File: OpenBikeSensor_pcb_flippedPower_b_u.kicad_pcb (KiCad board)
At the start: 2 copper layers, 58.2 x 62.2 mm, 34 parts, among them J1 Conn_01x02_Male, J10 Conn_02x03_Odd_Even, J11 Conn_01x02_Male, J2 Conn_01x04_Female, J3 Conn_01x04_Male, J4 Conn_01x04_Male, J5 Conn_01x05_Male, J6 Conn_01x02_Male, J7 Conn_01x06_Male, J8 Conn_01x06_Male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

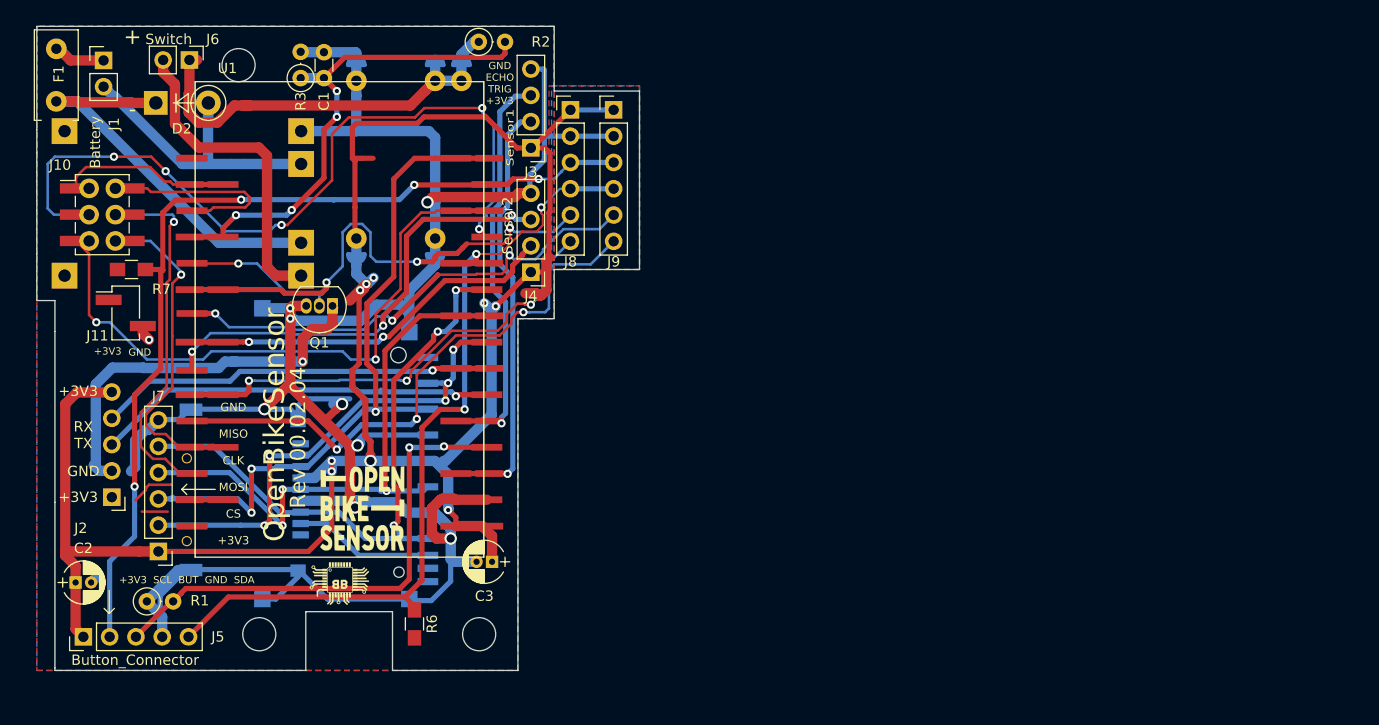
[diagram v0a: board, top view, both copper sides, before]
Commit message: add new US sensor boards to the PCB
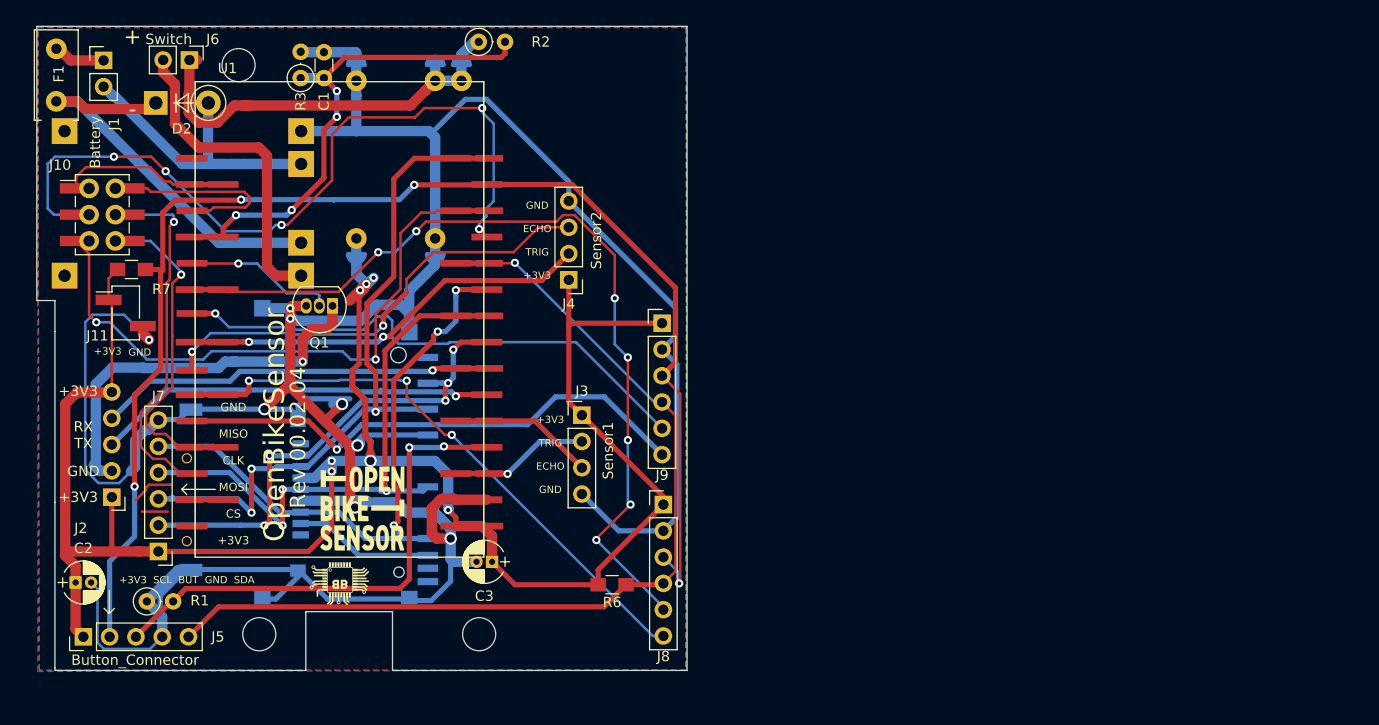
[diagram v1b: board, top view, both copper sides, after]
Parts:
- moved J8 39.2 mm to (82.8, 93.2)
- moved J3 26.3 mm to (74.9, 84.6), turned to 0 degrees
- moved J9 21.1 mm to (82.7, 75.7)
- moved R6 19.5 mm to (77.9, 101.0), turned to 180 degrees
- moved J4 3.74 mm to (73.7, 71.5)
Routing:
- net GND: track 263.4 -> 337.7 mm, vias 9 -> 8
- net SCL: track 90.5 -> 134.8 mm
- net GPIO_INT_1: track 48.5 -> 84.8 mm, vias 3 -> 7
- net TRIG1: track 41.6 -> 13.5 mm
- net ECHO1: track 39.0 -> 15.0 mm, vias 1 -> 0
- net +3V3: track 236.2 -> 223.8 mm, vias 9 -> 7
- net XSHUT_1: track 45.7 -> 58.1 mm
- net SDA: track 84.9 -> 93.7 mm, vias 3 -> 1
- net GPIO_INT_2: track 47.7 -> 52.2 mm, vias 3 -> 1
- net XSHUT_2: track 55.3 -> 51.4 mm, vias 3 -> 1
- net TRIG2: track 37.3 -> 40.2 mm
- net ECHO2: track 46.3 -> 44.6 mm, vias 3 -> 2
- net +BATT: track 38.2 -> 39.3 mm
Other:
- board size 58.2 x 62.2 mm -> 62.8 x 62.2 mm
- board text added: "+3V3 TRIG ECHO GND"

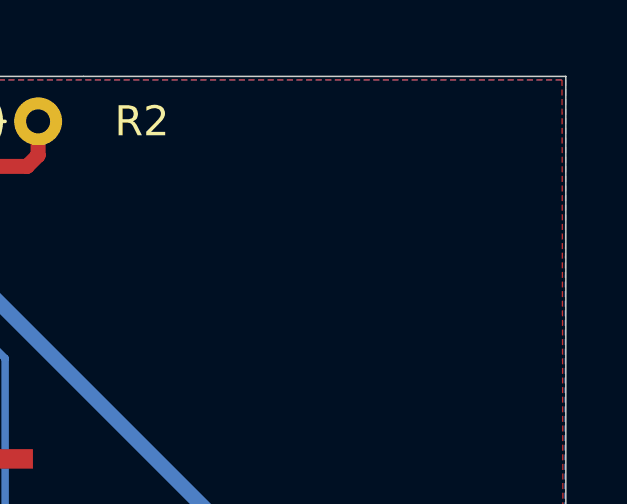
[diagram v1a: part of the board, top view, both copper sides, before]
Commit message: deleted 2 orphan traces
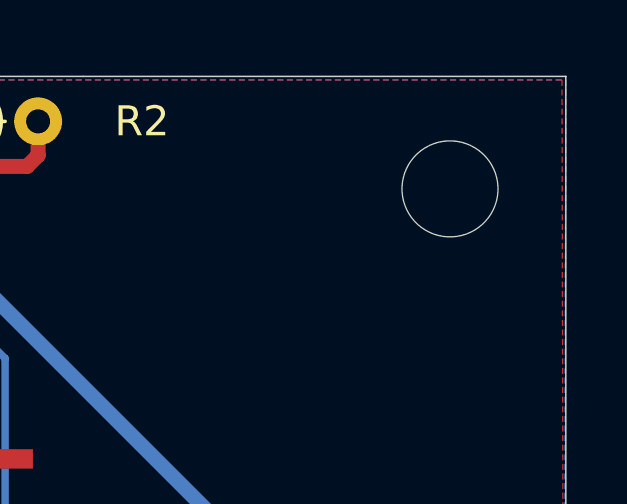
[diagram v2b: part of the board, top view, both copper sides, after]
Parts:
- added REF**: MountingHole_3.2mm_M3_DIN965, Mounting_Holes:MountingHole_3.2mm_M3_DIN965, F.Cu at (81.2, 50.7)
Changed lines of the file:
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@@
-(kicad_pcb (version 20171130) (host pcbnew "(5.1.6)-1")
+(kicad_pcb (version 20171130) (host pcbnew "(5.1.4)-1")
   (general
     (thickness 1.6)
@@
     (tracks 749)
     (zones 0)
-    (modules 34)
+    (modules 35)
     (nets 45)
   )
@@
   )
   (setup
-    (last_trace_width 1)
+    (last_trace_width 0.25)
     (user_trace_width 0.2)
     (user_trace_width 0.5)
@@
     (add_net XSHUT_1)
     (add_net XSHUT_2)
+  )
+  (module Mounting_Holes:MountingHole_3.2mm_M3_DIN965 locked (layer F.Cu)
+    (at 81.2292 50.7492)
+    (descr "Mounting Hole 3.2mm, no annular, M3, DIN965")
+    (tags "mounting hole 3.2mm no annular m3 din965")
+    (attr virtual)
+    (fp_text reference REF** (at 0 -3.8) (layer F.SilkS) hide
+      (effects (font (size 1 1) (thickness 0.15)))
+    )
+    (fp_text value MountingHole_3.2mm_M3_DIN965 (at 0 3.8) (layer F.Fab)
+      (effects (font (size 1 1) (thickness 0.15)))
+    )
+    (fp_text user %R (at 0.3 0) (layer F.Fab)
+      (effects (font (size 1 1) (thickness 0.15)))
+    )
+    (fp_circle (center 0 0) (end 3.05 0) (layer F.CrtYd) (width 0.05))
+    (fp_circle (center 0 0) (end 2.8 0) (layer Cmts.User) (width 0.15))
+    (pad 1 np_thru_hole circle (at 0 0) (size 3.2 3.2) (drill 3.2) (layers *.Cu *.Mask))
+    (model "${OPENBIKE}/hex_socket_button_head_M3x05 (1).step"
+      (at (xyz 0 0 0))
+      (scale (xyz 1 1 1))
+      (rotate (xyz 0 0 0))
+    )
   )
   (module Diodes_THT:D_DO-41_SOD81_P5.08mm_Vertical_KathodeUp (layer F.Cu)
@@
     )
     (pad 1 np_thru_hole circle (at 0 0) (size 3.2 3.2) (drill 3.2) (layers *.Cu *.Mask))
+    (model "${OPENBIKE}/hex_socket_button_head_M3x05 (1).step"
+      (at (xyz 0 0 0))
+      (scale (xyz 1 1 1))
+      (rotate (xyz 0 0 0))
+    )
   )
   (module Mounting_Holes:MountingHole_3.2mm_M3_DIN965 locked (layer F.Cu)
@@
     )
     (pad 1 np_thru_hole circle (at 0 0) (size 3.2 3.2) (drill 3.2) (layers *.Cu *.Mask))
+    (model "${OPENBIKE}/hex_socket_button_head_M3x05 (1).step"
+      (at (xyz 0 0 0))
+      (scale (xyz 1 1 1))
+      (rotate (xyz 0 0 0))
+    )
   )
   (module Mounting_Holes:MountingHole_3.2mm_M3_DIN965 locked (layer F.Cu)
@@
     )
     (pad 1 np_thru_hole circle (at 0 0) (size 3.2 3.2) (drill 3.2) (layers *.Cu *.Mask))
+    (model "${OPENBIKE}/hex_socket_button_head_M3x05 (1).step"
+      (at (xyz 0 0 0))
+      (scale (xyz 1 1 1))
+      (rotate (xyz 0 0 0))
+    )
   )
   (module SD_CARD:SD_CARD-XUNPU-SD-101_C266601 locked (layer B.Cu)

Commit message: new _u version
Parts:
- removed the REF** at (81.2, 50.7)
- removed the REF** at (41.8, 50.8)
- removed the REF** at (43.8, 105.8)
- added G***: LOGO, HLRS_LogoBack:HLRS_LogoBack, F.Cu at (80.3, 64.1)
- added G***: LOGO, HLRS_Logo:HLRS_Logo, F.Cu at (49.3, 109.1)
- D2: footprint Diodes_THT:D_DO-41_SOD81_P5.08mm_Vertical_KathodeUp -> Diode_THT:D_DO-41_SOD81_P10.16mm_Horizontal
- J5: footprint Pin_Headers:Pin_Header_Straight_1x05_Pitch2.54mm -> Connector_JST:JST_XH_B5B-XH-AM_1x05_P2.50mm_Vertical
- R1, R3: footprint Resistors_THT:R_Axial_DIN0207_L6.3mm_D2.5mm_P2.54mm_Vertical -> Resistor_THT:R_Axial_DIN0207_L6.3mm_D2.5mm_P10.16mm_Horizontal
- R2: footprint Resistors_THT:R_Axial_DIN0207_L6.3mm_D2.5mm_P2.54mm_Vertical -> Resistor_THT:R_Axial_DIN0207_L6.3mm_D2.5mm_P15.24mm_Horizontal
- moved REF** 55.4 mm to (82.9, 53.3)
- moved G*** 46.1 mm to (71.6, 55.4), turned to 270 degrees
- moved G*** 22.9 mm to (73.8, 95.9)
- moved G*** 20.7 mm to (72.0, 102.4), turned to 90 degrees
- moved R1 20.2 mm to (52.8, 105.7), turned to 180 degrees
- moved G*** 16.3 mm to (62.9, 107.1)
- moved C1 8.03 mm to (42.5, 49.0), turned to 180 degrees
- moved R6 3.94 mm to (77.9, 104.9)
- moved M1 1.82 mm to (35.2, 64.1)
- moved R3 1.71 mm to (49.4, 51.6), turned to 270 degrees
- moved J5 1.44 mm to (27.6, 107.2), turned to 0 degrees
- moved D2 1.25 mm to (32.5, 54.2)
- moved R2 0.87 mm to (65.8, 48.8), turned to 180 degrees
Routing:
- net TX: track 75.3 -> 52.2 mm, vias 5 -> 2
- net BUTTON: track 49.0 -> 61.5 mm
- net Net-(C1-Pad1): track 48.4 -> 39.2 mm, vias 4 -> 3
- net +3V3: track 223.8 -> 229.9 mm
- net SDA: track 93.7 -> 99.3 mm
- net Net-(J6-Pad2): track 31.2 -> 26.0 mm
- net +BATT: track 39.3 -> 35.8 mm
- net SCL: track 134.8 -> 131.5 mm
- net XSHUT_1: track 58.1 -> 60.0 mm
- net GND: track 337.7 -> 335.9 mm, vias 8 -> 10
- net -BATT: track 28.5 -> 27.4 mm
- net +VDC: track 41.2 -> 40.2 mm
- net GPIO_INT_2: track 52.2 -> 52.7 mm
- net GPS_GND_CONT: track 14.6 -> 14.2 mm, vias 1 -> 0
- net GPIO_INT_1: track 84.8 -> 85.1 mm, vias 7 -> 3
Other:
- board size 62.8 x 62.2 mm -> 65.7 x 64.6 mm
- board text added: "12"
- board text added: "13"
- board text added: "RX"
- board text added: "Rev 00.03.08"
- board text added: "TX"
- board text added: "VN"
- board text added: "VP"
- board text removed: "Rev 00.02.04"

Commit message: fixed boundary
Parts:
- removed the G*** at (80.3, 64.1)
- added G***: LOGO, HLRS_Logo:HLRS_LogoBack, F.Cu at (79.4, 63.9)

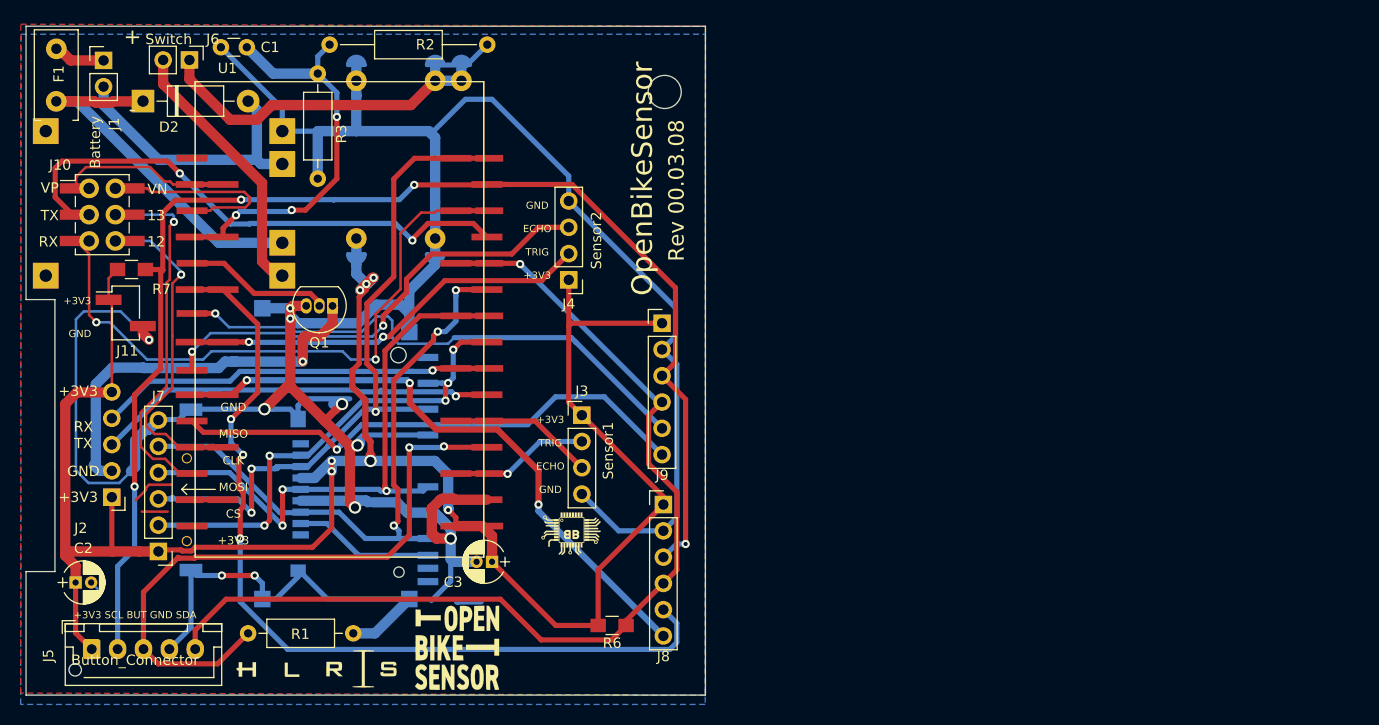
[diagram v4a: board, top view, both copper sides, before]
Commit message: added more srew holes improved ground/vcc planes updated 3D Models
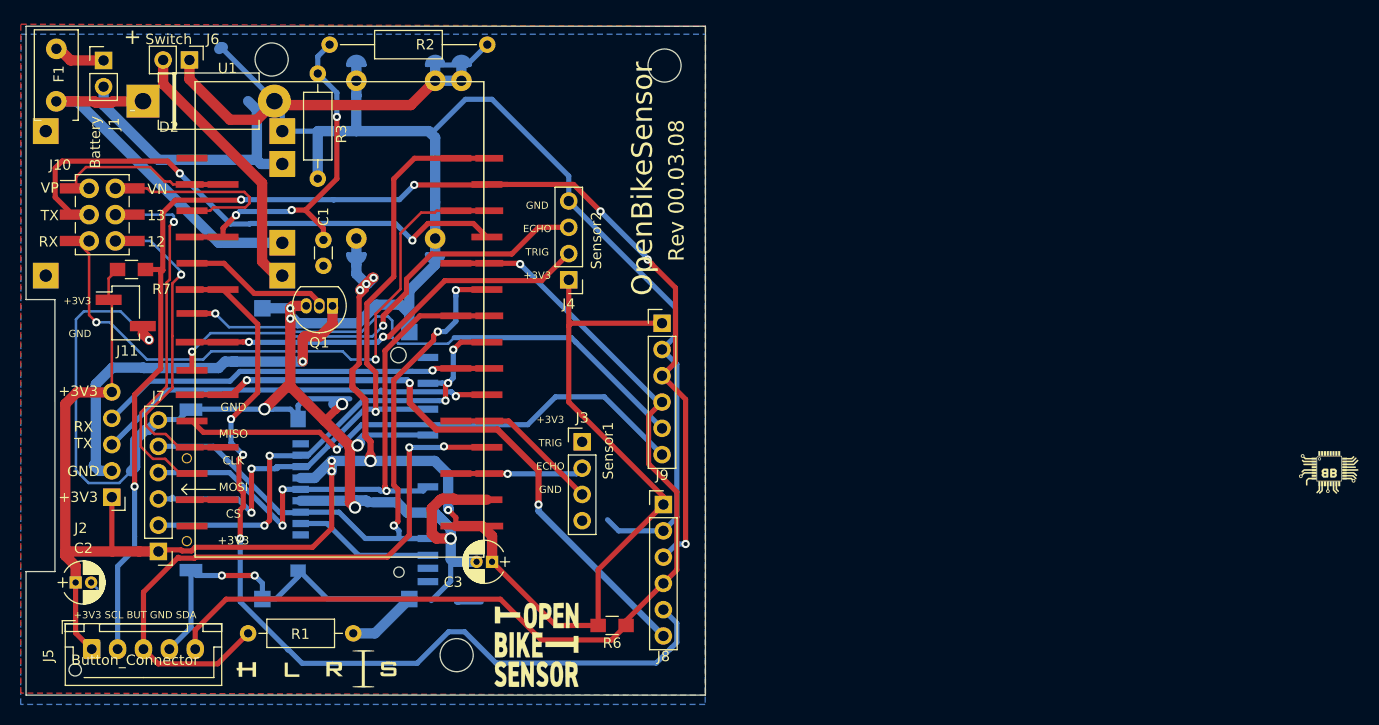
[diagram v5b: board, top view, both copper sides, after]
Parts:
- added REF**: MountingHole_3.2mm_M3_DIN965, Mounting_Holes:MountingHole_3.2mm_M3_DIN965, F.Cu at (44.9, 50.2)
- added REF**: MountingHole_3.2mm_M3_DIN965, Mounting_Holes:MountingHole_3.2mm_M3_DIN965, F.Cu at (62.8, 107.8)
- D2: footprint Diode_THT:D_DO-41_SOD81_P10.16mm_Horizontal -> Diode_THT:D_DO-201AD_P12.70mm_Horizontal
- moved G*** 73.5 mm to (147.0, 90.0)
- moved C1 20.0 mm to (49.9, 67.6), turned to 270 degrees
- moved G*** 7.68 mm to (70.5, 106.8)
- moved J3 2.58 mm to (75.0, 87.2)
- moved REF** 2.55 mm to (82.9, 50.8)
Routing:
- net (no net): track 6.64 -> 0.00 mm
- net Net-(C1-Pad1): track 39.2 -> 34.9 mm
- net GPIO_INT_1: track 85.1 -> 89.0 mm
- net GND: track 335.9 -> 332.4 mm
- net ECHO1: track 15.0 -> 16.1 mm
- net TRIG1: track 13.5 -> 12.4 mm
- net SCL: track 131.5 -> 131.6 mm, vias 4 -> 6

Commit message: fixed mistake in esp footprint fixed problem with diode
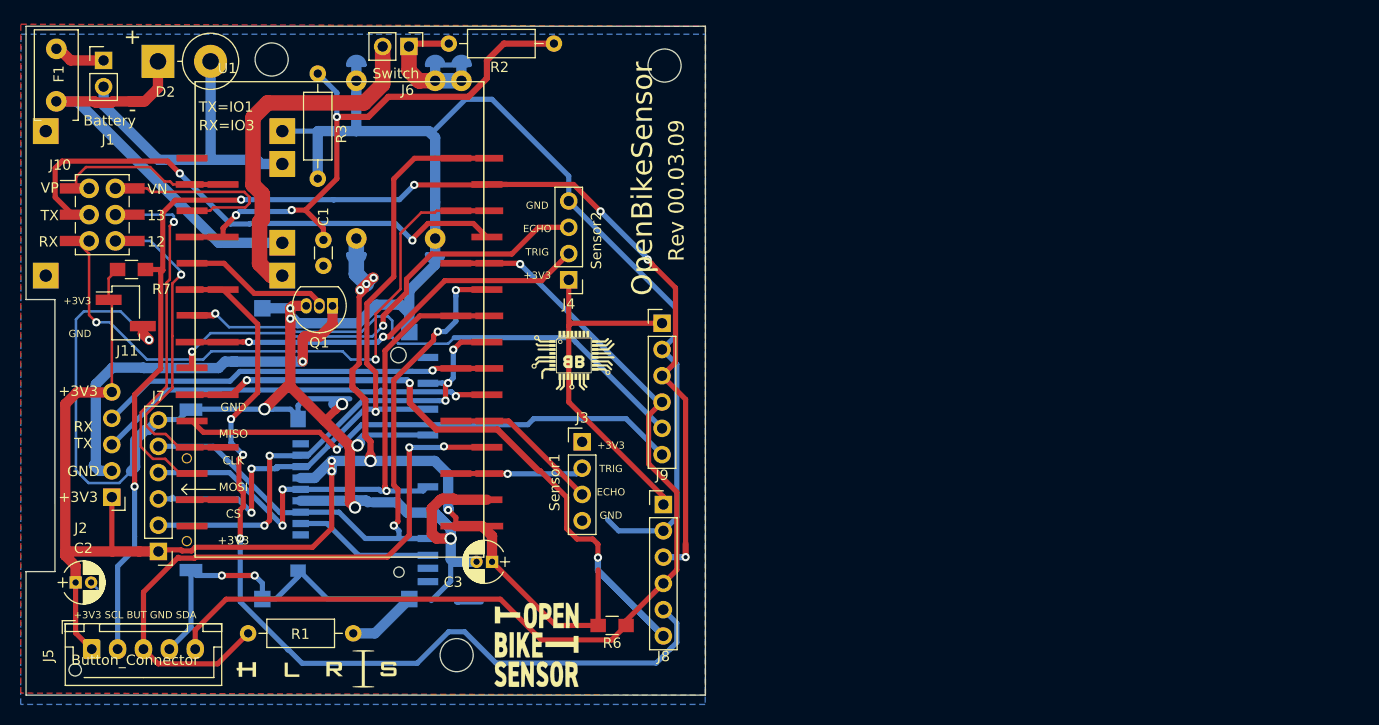
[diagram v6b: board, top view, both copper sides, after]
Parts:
- D2: footprint Diode_THT:D_DO-201AD_P12.70mm_Horizontal -> Diode_THT:D_DO-201AD_P5.08mm_Vertical_KathodeUp
- G***: footprint Custom_logo:BB_5x4 -> Custom_logo:BB_8x6
- R2: footprint Resistor_THT:R_Axial_DIN0207_L6.3mm_D2.5mm_P15.24mm_Horizontal -> Resistor_THT:R_Axial_DIN0207_L6.3mm_D2.5mm_P10.16mm_Horizontal
- moved G*** 73.9 mm to (74.0, 79.1)
- moved J6 21.3 mm to (58.2, 48.9)
- moved D2 4.11 mm to (34.0, 50.4)
- moved R2 3.72 mm to (62.1, 48.7), turned to 0 degrees
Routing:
- net +VDC: track 40.2 -> 17.9 mm
- net Net-(C1-Pad1): track 34.9 -> 56.5 mm
- net XSHUT_1: track 60.0 -> 71.2 mm
- net GND: track 332.4 -> 321.4 mm
- net Net-(J6-Pad2): track 26.0 -> 35.4 mm
- net +BATT: track 35.8 -> 41.6 mm
- net +3V3: track 229.9 -> 224.4 mm
- net -BATT: track 27.4 -> 31.0 mm
- net XSHUT_2: track 51.4 -> 49.7 mm
- net SCL: track 131.6 -> 132.3 mm
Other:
- board text added: "+3,3V GND SCL SDA INT IO32 XSHUT"
- board text added: "+3,3V GND SCL SDA INT IO33 XSHUT"
- board text added: "IO14"
- board text added: "IO27"
- board text added: "RX=IO3"
- board text added: "Rev 00.03.09"
- board text added: "TX=IO1"
- board text removed: "+3,3V GND SCL SDA INT XSHUT"
- board text removed: "Rev 00.03.08"
